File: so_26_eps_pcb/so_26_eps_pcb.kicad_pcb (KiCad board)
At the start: 4 copper layers, 90.2 x 95.9 mm, 85 parts, among them J1 Conn_02x12_Odd_Even, J2 Conn_01x02, J3 Conn_01x02, SW1 SW_SPDT

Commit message: Rev 1 of placing components on pcb
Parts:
- moved D5 156.4 mm to (107.7, 64.8)
- moved R12 156.4 mm to (107.7, 71.7)
- moved R13 155.1 mm to (122.7, 72.0)
- moved D6 155.1 mm to (122.7, 65.9)
- moved TP34 154.8 mm to (101.6, 78.8)
- moved TP35 154.8 mm to (123.0, 77.0)
- moved C7 149.8 mm to (73.1, 97.1)
- moved R3 147.0 mm to (73.1, 101.9)
- moved R4 136.7 mm to (73.9, 62.0)
- moved D1 135.1 mm to (100.8, 97.2), turned to -90 degrees
- moved TP18 133.8 mm to (94.2, 142.8)
- moved TP17 133.0 mm to (94.2, 132.4)
- moved TP16 131.1 mm to (94.2, 137.2)
- moved C8 129.6 mm to (73.9, 55.7)
- moved C6 127.9 mm to (73.9, 37.2)
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
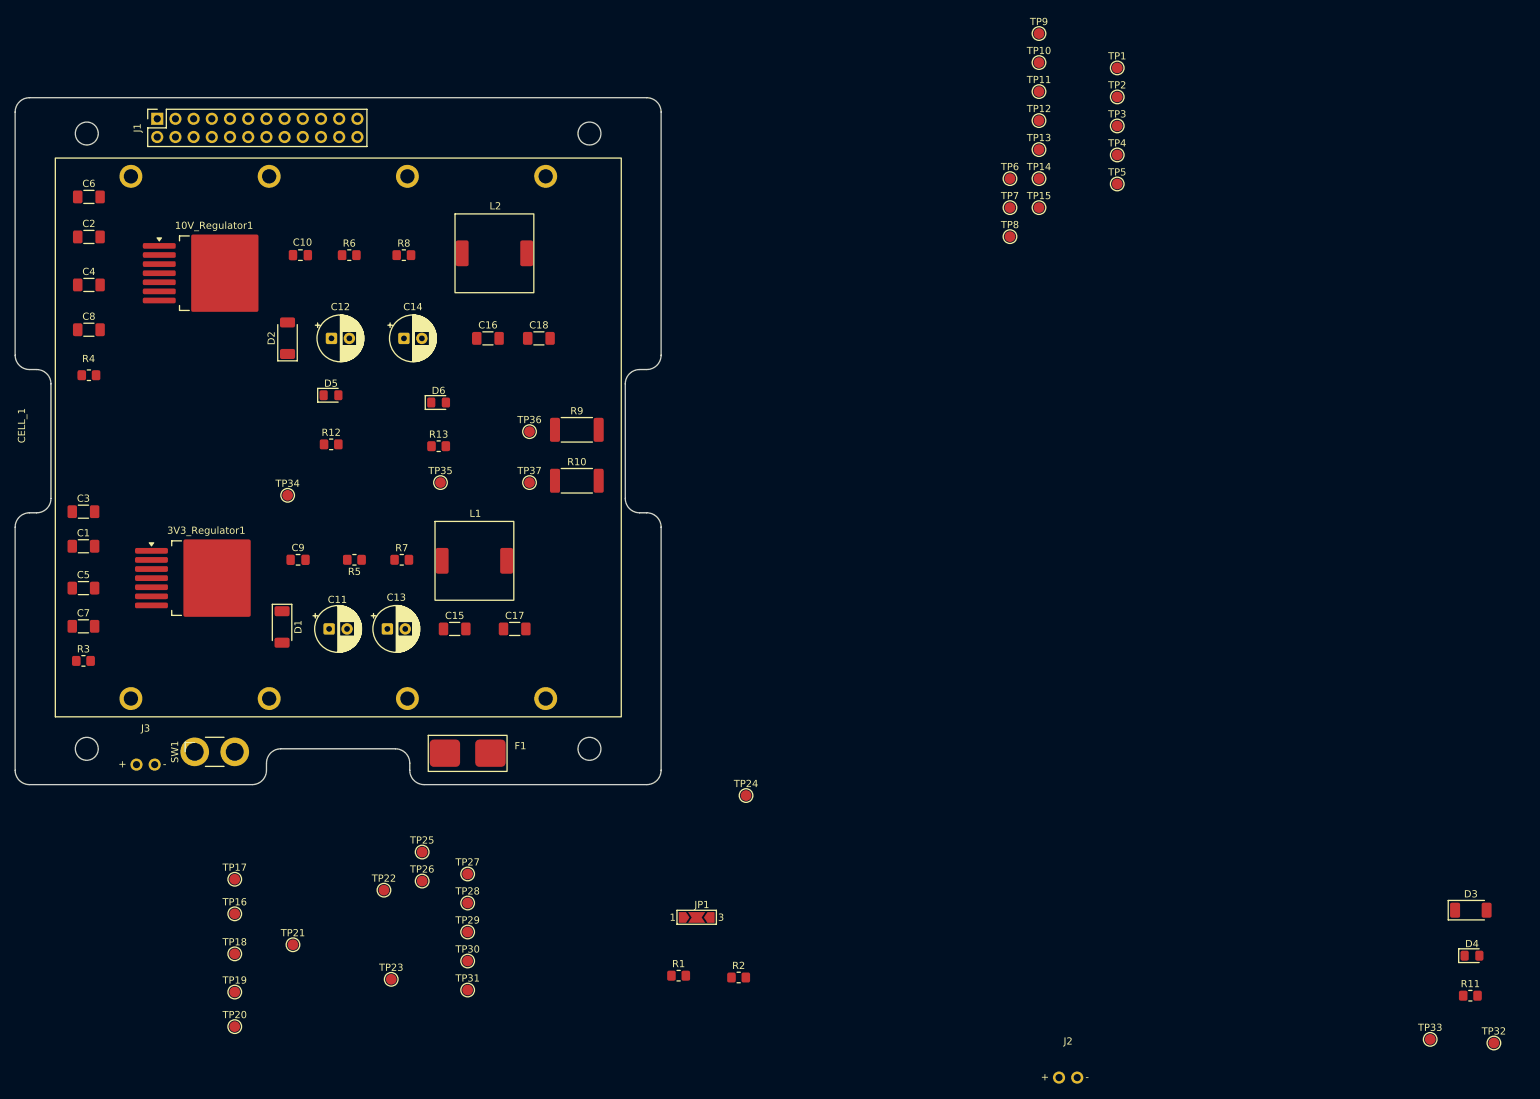
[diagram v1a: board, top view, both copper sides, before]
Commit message: Changed the place on some of the components on the PCB
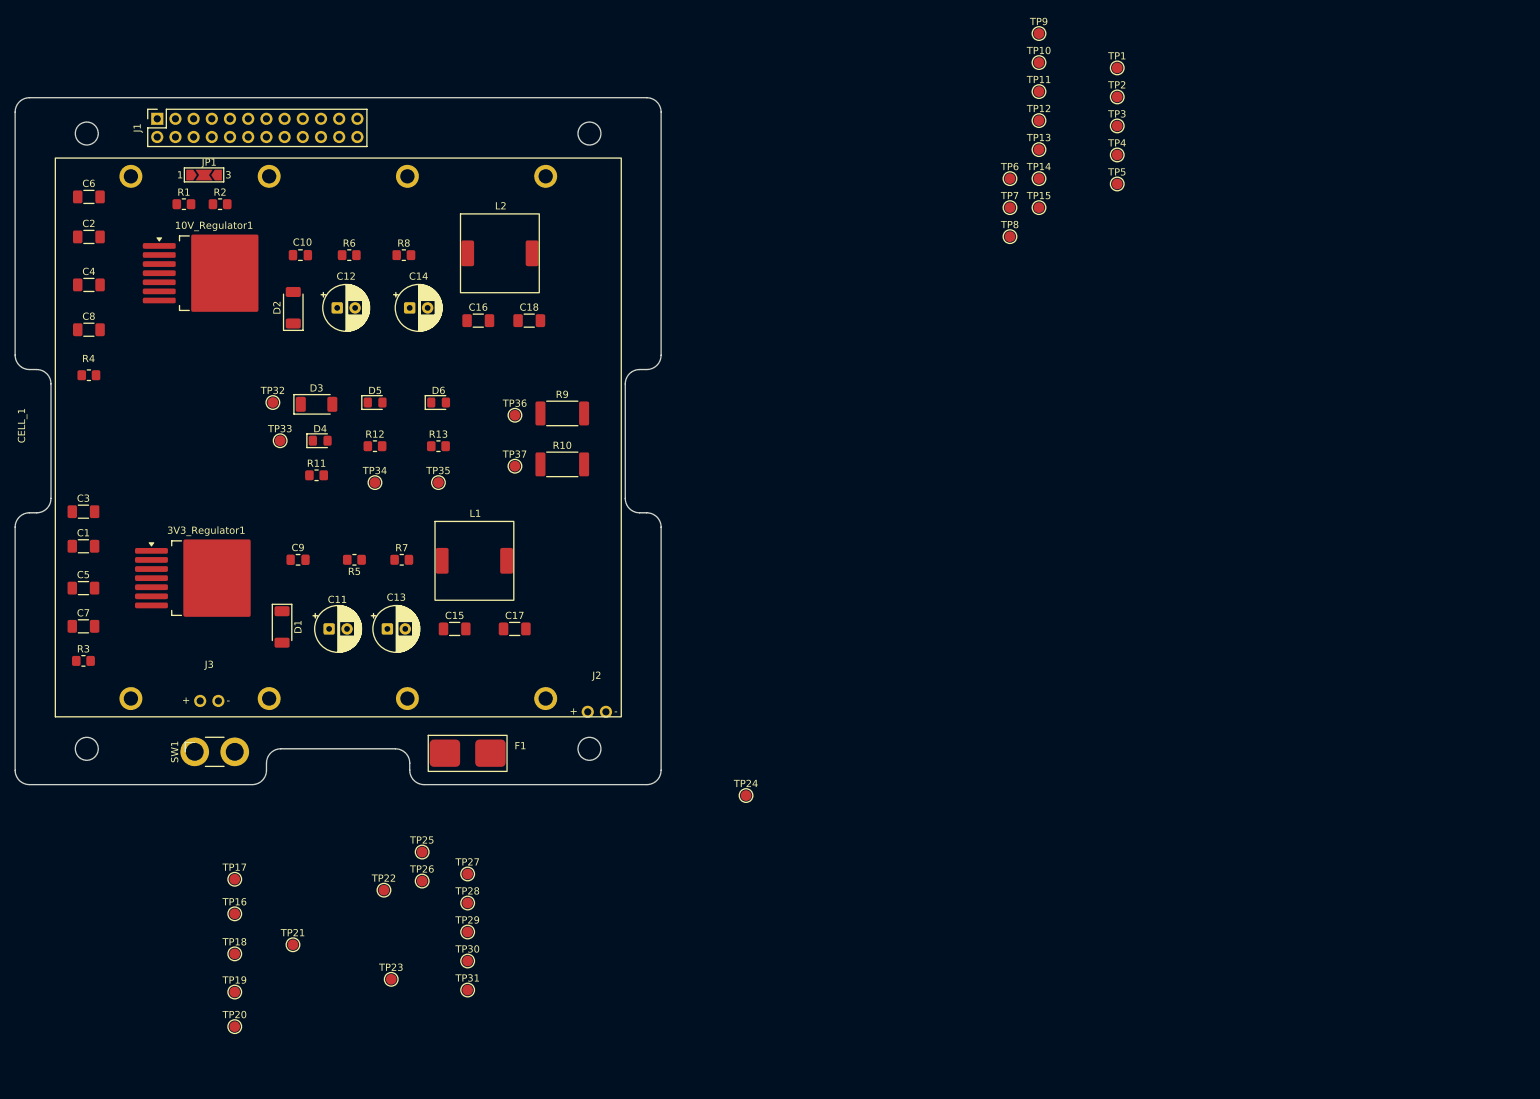
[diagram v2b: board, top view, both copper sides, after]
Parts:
- moved TP32 192.5 mm to (99.6, 65.9)
- moved TP33 181.0 mm to (100.6, 71.2)
- moved R11 176.7 mm to (105.7, 76.0)
- moved D4 176.1 mm to (106.2, 71.2)
- moved D3 175.9 mm to (105.7, 66.1)
- moved R2 130.0 mm to (92.2, 38.2)
- moved R1 127.9 mm to (87.1, 38.2)
- moved JP1 124.4 mm to (89.9, 34.1)
- moved J2 83.3 mm to (144.8, 104.5)
- moved J3 12.6 mm to (90.7, 102.9)
- moved TP34 12.3 mm to (113.8, 77.0)
- moved D5 6.24 mm to (113.8, 65.9)
- moved R12 6.12 mm to (113.8, 72.0)
- moved C14 4.33 mm to (118.7, 52.6)
- moved D2 4.33 mm to (102.4, 52.6)
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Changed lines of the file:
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@@
 	(footprint "TestPoint:TestPoint_Pad_D1.5mm"
 		(layer "F.Cu")
-		(at 101.618 78.809)
+		(at 113.808 77.031)
 		(descr "SMD pad as test Point, diameter 1.5mm")
 		(tags "test point SMD pad")
@@
 	(footprint "TestPoint:TestPoint_Pad_D1.5mm"
 		(layer "F.Cu")
-		(at 261.112 154.755)
+		(at 100.575 71.189)
 		(descr "SMD pad as test Point, diameter 1.5mm")
 		(tags "test point SMD pad")
@@
 	(footprint "Capacitor_THT:CP_Radial_D6.3mm_P2.50mm"
 		(layer "F.Cu")
-		(at 107.736 56.9015)
+		(at 108.538 52.647)
 		(descr "CP, Radial series, Radial, pin pitch=2.50mm, diameter=6.3mm, height=7mm, Electrolytic Capacitor")
 		(tags "CP Radial series Radial pin pitch 2.50mm diameter 6.3mm height 7mm Electrolytic Capacitor")
@@
 	(footprint "Resistor_SMD:R_0805_2012Metric_Pad1.20x1.40mm_HandSolder"
 		(layer "F.Cu")
-		(at 156.194 145.865)
+		(at 87.138 38.169)
 		(descr "Resistor SMD 0805 (2012 Metric), square (rectangular) end terminal, IPC-7351 nominal with elongated pad for handsoldering. (Body size source: IPC-SM-782 page 72, https://www.pcb-3d.com/wordpress/wp-content/uploads/ipc-sm-782a_amendment_1_and_2.pdf), generated with kicad-footprint-generator")
 		(tags "resistor handsolder")
@@
 	(footprint "TestPoint:TestPoint_Pad_D1.5mm"
 		(layer "F.Cu")
-		(at 270.002 155.263)
+		(at 99.559 65.855)
 		(descr "SMD pad as test Point, diameter 1.5mm")
 		(tags "test point SMD pad")
@@
 	(footprint "LED_SMD:LED_0805_2012Metric_Pad1.15x1.40mm_HandSolder"
 		(layer "F.Cu")
-		(at 107.671 64.839)
+		(at 113.8305 65.855)
 		(descr "LED SMD 0805 (2012 Metric), square (rectangular) end terminal, IPC-7351 nominal, (Body size source: https://docs.google.com/spreadsheets/d/1BsfQQcO9C6DZCsRaXUlFlo91Tg2WpOkGARC1WS5S8t0/edit?usp=sharing), generated with kicad-footprint-generator")
 		(tags "LED handsolder")
@@
 	(footprint "LED_SMD:LED_0805_2012Metric_Pad1.15x1.40mm_HandSolder"
 		(layer "F.Cu")
-		(at 266.945 143.071)
+		(at 106.163 71.189)
 		(descr "LED SMD 0805 (2012 Metric), square (rectangular) end terminal, IPC-7351 nominal, (Body size source: https://docs.google.com/spreadsheets/d/1BsfQQcO9C6DZCsRaXUlFlo91Tg2WpOkGARC1WS5S8t0/edit?usp=sharing), generated with kicad-footprint-generator")
 		(tags "LED handsolder")
@@
 	(footprint "Jumper:SolderJumper-3_P2.0mm_Open_TrianglePad1.0x1.5mm_NumberLabels"
 		(layer "F.Cu")
-		(at 158.718 137.737)
+		(at 89.948 34.105)
 		(descr "SMD Solder Jumper, 1x1.5mm Triangular Pads, 0.3mm gap, open, labeled with numbers")
 		(tags "solder jumper open")
@@
 	(footprint "Resistor_SMD:R_2512_6332Metric_Pad1.40x3.35mm_HandSolder"
 		(layer "F.Cu")
-		(at 141.988 76.777)
+		(at 139.954 74.491)
 		(descr "Resistor SMD 2512 (6332 Metric), square (rectangular) end terminal, IPC-7351 nominal with elongated pad for handsoldering. (Body size source: IPC-SM-782 page 72, https://www.pcb-3d.com/wordpress/wp-content/uploads/ipc-sm-782a_amendment_1_and_2.pdf), generated with kicad-footprint-generator")
 		(tags "resistor handsolder")
@@
 	(footprint "Diode_SMD:D_SOD-128"
 		(layer "F.Cu")
-		(at 101.6 56.879 90)
+		(at 102.402 52.6245 90)
 		(descr "D_SOD-128 (CFP5 SlimSMAW), https://assets.nexperia.com/documents/outline-drawing/SOD128.pdf")
 		(tags "D_SOD-128")
@@
 	(footprint "TestPoint:TestPoint_Pad_D1.5mm"
 		(layer "F.Cu")
-		(at 122.954 77.031)
+		(at 122.6665 77.031)
 		(descr "SMD pad as test Point, diameter 1.5mm")
 		(tags "test point SMD pad")
@@
 	(footprint "Myfootprints:01x02_header"
 		(layer "F.Cu")
-		(at 210.566 155.517)
+		(at 144.78 104.463)
 		(property "Reference" "J2"
 			(at 0 -0.5 0)
@@
 	(footprint "Diode_SMD:D_SOD-128"
 		(layer "F.Cu")
-		(at 266.786 136.721)
+		(at 105.655 66.109)
 		(descr "D_SOD-128 (CFP5 SlimSMAW), https://assets.nexperia.com/documents/outline-drawing/SOD128.pdf")
 		(tags "D_SOD-128")
@@
 	(footprint "Myfootprints:SRU1048 Inductor"
 		(layer "F.Cu")
-		(at 130.611 38.931)
+		(at 131.373 38.931)
 		(property "Reference" "L2"
 			(at 0 -0.5 0)
@@
 	(footprint "Capacitor_SMD:C_1206_3216Metric_Pad1.33x1.80mm_HandSolder"
 		(layer "F.Cu")
-		(at 129.5785 56.9015)
+		(at 128.2315 54.425)
 		(descr "Capacitor SMD 1206 (3216 Metric), square (rectangular) end terminal, IPC-7351 nominal with elongated pad for handsoldering. (Body size source: IPC-SM-782 page 76, https://www.pcb-3d.com/wordpress/wp-content/uploads/ipc-sm-782a_amendment_1_and_2.pdf), generated with kicad-footprint-generator")
 		(tags "capacitor handsolder")
@@
 	(footprint "Capacitor_SMD:C_1206_3216Metric_Pad1.33x1.80mm_HandSolder"
 		(layer "F.Cu")
-		(at 136.6905 56.9015)
+		(at 135.3435 54.425)
 		(descr "Capacitor SMD 1206 (3216 Metric), square (rectangular) end terminal, IPC-7351 nominal with elongated pad for handsoldering. (Body size source: IPC-SM-782 page 76, https://www.pcb-3d.com/wordpress/wp-content/uploads/ipc-sm-782a_amendment_1_and_2.pdf), generated with kicad-footprint-generator")
 		(tags "capacitor handsolder")
@@
 	(footprint "Resistor_SMD:R_0805_2012Metric_Pad1.20x1.40mm_HandSolder"
 		(layer "F.Cu")
-		(at 107.696 71.697)
+		(at 113.808 71.951)
 		(descr "Resistor SMD 0805 (2012 Metric), square (rectangular) end terminal, IPC-7351 nominal with elongated pad for handsoldering. (Body size source: IPC-SM-782 page 72, https://www.pcb-3d.com/wordpress/wp-content/uploads/ipc-sm-782a_amendment_1_and_2.pdf), generated with kicad-footprint-generator")
 		(tags "resistor handsolder")
@@
 	(footprint "Resistor_SMD:R_0805_2012Metric_Pad1.20x1.40mm_HandSolder"
 		(layer "F.Cu")
-		(at 266.716 148.659)
+		(at 105.655 76.015)
 		(descr "Resistor SMD 0805 (2012 Metric), square (rectangular) end terminal, IPC-7351 nominal with elongated pad for handsoldering. (Body size source: IPC-SM-782 page 72, https://www.pcb-3d.com/wordpress/wp-content/uploads/ipc-sm-782a_amendment_1_and_2.pdf), generated with kicad-footprint-generator")
 		(tags "resistor handsolder")
@@
 	(footprint "Resistor_SMD:R_0805_2012Metric_Pad1.20x1.40mm_HandSolder"
 		(layer "F.Cu")
-		(at 122.698 71.951)
+		(at 122.6665 71.951)
 		(descr "Resistor SMD 0805 (2012 Metric), square (rectangular) end terminal, IPC-7351 nominal with elongated pad for handsoldering. (Body size source: IPC-SM-782 page 72, https://www.pcb-3d.com/wordpress/wp-content/uploads/ipc-sm-782a_amendment_1_and_2.pdf), generated with kicad-footprint-generator")
 		(tags "resistor handsolder")
@@
 	(footprint "Myfootprints:01x02_header"
 		(layer "F.Cu")
-		(at 81.788 111.829)
+		(at 90.678 102.939)
 		(property "Reference" "J3"
 			(at 0 -0.5 0)
@@
 	(footprint "Resistor_SMD:R_2512_6332Metric_Pad1.40x3.35mm_HandSolder"
 		(layer "F.Cu")
-		(at 141.988 69.665)
+		(at 139.954 67.379)
 		(descr "Resistor SMD 2512 (6332 Metric), square (rectangular) end terminal, IPC-7351 nominal with elongated pad for handsoldering. (Body size source: IPC-SM-782 page 72, https://www.pcb-3d.com/wordpress/wp-content/uploads/ipc-sm-782a_amendment_1_and_2.pdf), generated with kicad-footprint-generator")
 		(tags "resistor handsolder")
@@
 	(footprint "TestPoint:TestPoint_Pad_D1.5mm"
 		(layer "F.Cu")
-		(at 135.382 69.919)
+		(at 133.348 67.633)
 		(descr "SMD pad as test Point, diameter 1.5mm")
 		(tags "test point SMD pad")
@@
 	(footprint "Resistor_SMD:R_0805_2012Metric_Pad1.20x1.40mm_HandSolder"
 		(layer "F.Cu")
-		(at 164.576 146.119)
+		(at 92.186 38.169)
 		(descr "Resistor SMD 0805 (2012 Metric), square (rectangular) end terminal, IPC-7351 nominal with elongated pad for handsoldering. (Body size source: IPC-SM-782 page 72, https://www.pcb-3d.com/wordpress/wp-content/uploads/ipc-sm-782a_amendment_1_and_2.pdf), generated with kicad-footprint-generator")
 		(tags "resistor handsolder")
@@
 	(footprint "TestPoint:TestPoint_Pad_D1.5mm"
 		(layer "F.Cu")
-		(at 135.382 77.031)
+		(at 133.348 74.745)
 		(descr "SMD pad as test Point, diameter 1.5mm")
 		(tags "test point SMD pad")
@@
 	(footprint "Capacitor_THT:CP_Radial_D6.3mm_P2.50mm"
 		(layer "F.Cu")
-		(at 117.856 56.9015)
+		(at 118.658 52.647)
 		(descr "CP, Radial series, Radial, pin pitch=2.50mm, diameter=6.3mm, height=7mm, Electrolytic Capacitor")
 		(tags "CP Radial series Radial pin pitch 2.50mm diameter 6.3mm height 7mm Electrolytic Capacitor")

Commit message: Started some rooting
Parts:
- removed TP1, TP10, TP11, TP12, TP13, TP14, TP15, TP16, TP17, TP18, TP19, TP2, TP20, TP21, TP22, TP23, TP24, TP25, TP26, TP27, TP28, TP29, TP3, TP30, TP31, TP32, TP33, TP34, TP35, TP36, TP37, TP4, TP5, TP6, TP8, TP9: ~, TestPoint:TestPoint_Pad_D1.5mm
- removed TP7: TestPoint_Small, TestPoint:TestPoint_Pad_D1.5mm
- 10V_Regulator1, 3V3_Regulator1, C1, C10, C11, C12, C13, C14, C15, C16, C17, C18, C2, C3, C4, C5, C6, C7, C8, C9, D1, D2, D3, D4, D5, D6, JP1, L1, L2, R1, R10, R11, R12, R13, R2, R3, R4, R5, R6, R7, R8, R9: moved to B.Cu
- moved JP1 66.2 mm to (89.9, 100.3)
- moved R7 65.8 mm to (72.9, 39.4), turned to 180 degrees
- moved C7 62.6 mm to (73.1, 34.5)
- moved L1 60.6 mm to (70.4, 62.5), turned to -90 degrees
- moved C6 60.1 mm to (73.9, 97.2), turned to 180 degrees
- moved C17 59.1 mm to (119.5, 39.9), turned to 180 degrees
- moved R5 58.8 mm to (72.9, 43.0)
- moved R1 58.0 mm to (87.1, 96.2)
- moved R2 58.0 mm to (92.2, 96.2)
- moved C15 57.6 mm to (127.9, 39.9), turned to 180 degrees
- moved L2 56.5 mm to (131.4, 95.4)
- moved R3 55.6 mm to (72.9, 46.3), turned to 180 degrees
- moved C11 51.7 mm to (117.9, 46.8)
- moved C13 51.7 mm to (126.0, 46.8)
- moved C2 48.9 mm to (73.9, 91.6), turned to 180 degrees
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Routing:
- net VBAT: track 0.00 -> 21.7 mm
- net Net-(3V3_Regulator1-SW): track 0.00 -> 17.2 mm
- net Net-(3V3_Regulator1-FB): track 0.00 -> 13.2 mm
- net Net-(3V3_Regulator1-BOOT): track 0.00 -> 10.4 mm
- net Net-(3V3_Regulator1-SS): track 0.00 -> 10.3 mm
- net Net-(3V3_Regulator1-IADJ): track 0.00 -> 10.2 mm
